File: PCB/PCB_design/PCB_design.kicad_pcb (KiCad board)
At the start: 2 copper layers, 66.5 x 66 mm, 53 parts, among them J2 Conn_01x03_Pin, J3 Conn_01x01_Pin, J4 Conn_01x01_Pin, J5 Conn_01x01_Pin, J6 Conn_01x01_Pin, J7 Conn_02x04_Counter_Clockwise, K1 Relay_SPST-NO, K2 Relay_SPST-NO, K3 Relay_SPST-NO, K4 Relay_SPST-NO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

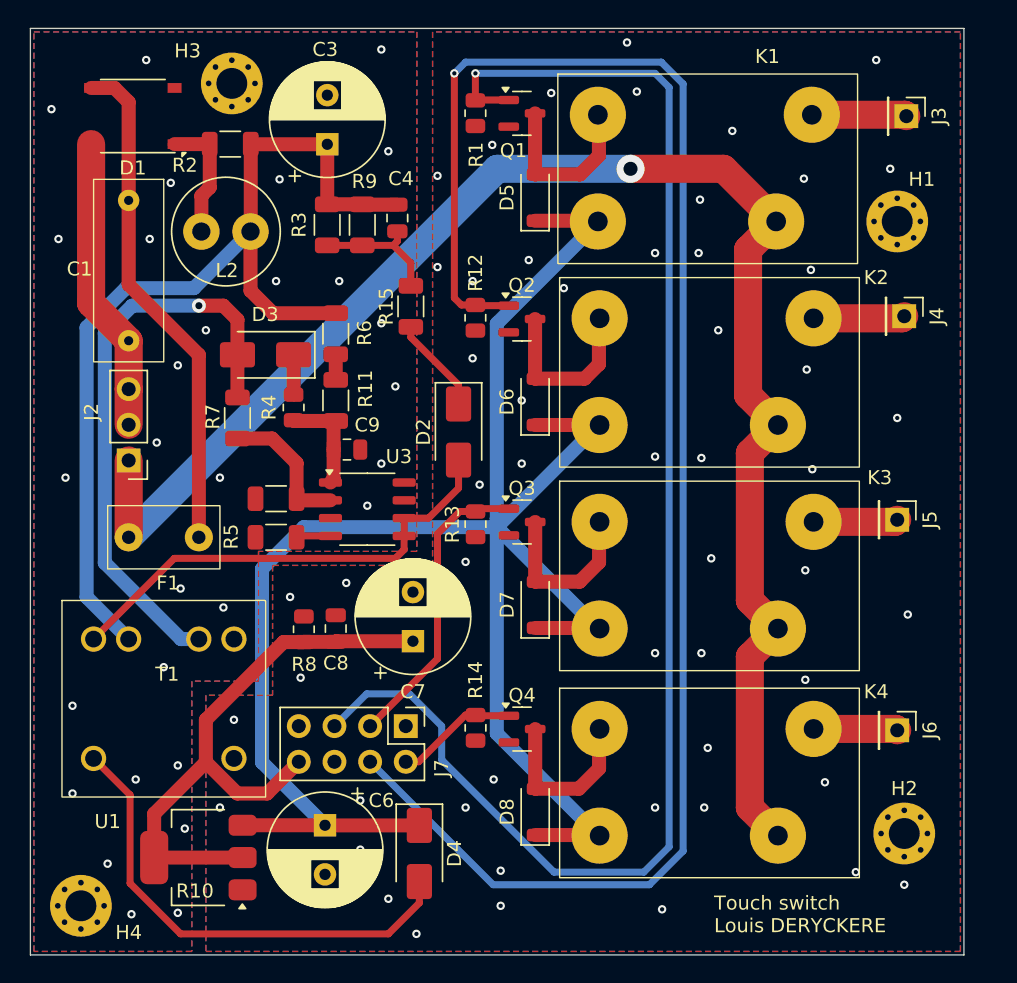
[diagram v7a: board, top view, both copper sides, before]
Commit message: Ajout pads AC & modifs pistes
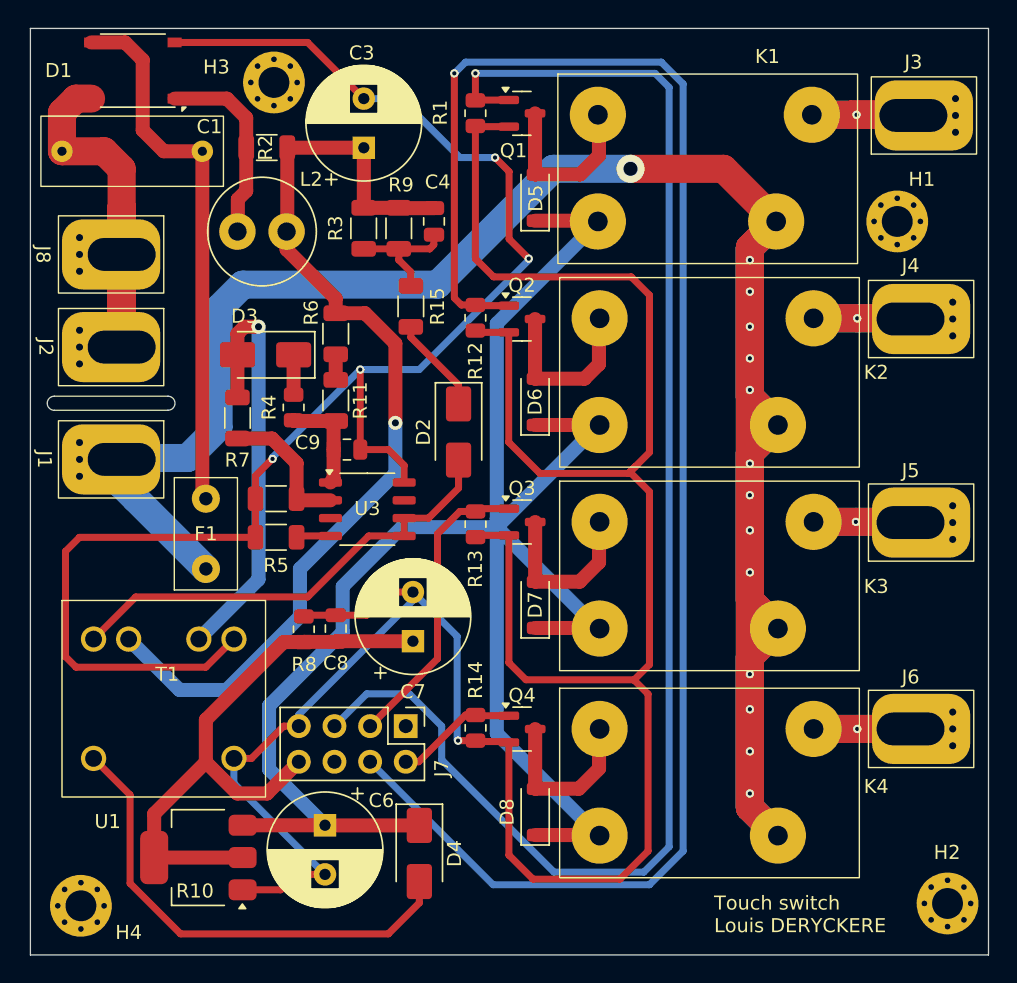
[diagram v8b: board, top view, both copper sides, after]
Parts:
- added J1: Conn_01x01_Pin, Touch_Switch_Custom:AC_pad, F.Cu at (100.0, 58.7)
- added J8: Conn_01x01_Pin, Touch_Switch_Custom:AC_pad, F.Cu at (100.0, 44.1)
- J2: value Conn_01x03_Pin -> Conn_01x01_Pin; footprint Connector_PinHeader_2.54mm:PinHeader_1x03_P2.54mm_Vertical -> Touch_Switch_Custom:AC_pad
- J3, J4, J5, J6: footprint Connector_PinHeader_2.54mm:PinHeader_1x01_P2.54mm_Vertical -> Touch_Switch_Custom:AC_pad
- moved J2 8.09 mm to (100.0, 50.7), turned to -90 degrees
- moved C1 6.31 mm to (105.8, 36.8), turned to 180 degrees
- moved H2 5.86 mm to (158.8, 90.3)
- moved D1 3.24 mm to (100.8, 31.0)
- moved F1 3.01 mm to (106.0, 64.0), turned to 90 degrees
- moved H3 3.00 mm to (110.8, 31.9)
- moved C4 2.62 mm to (122.2, 41.7)
- moved R2 2.61 mm to (110.3, 36.5)
- moved C3 2.61 mm to (117.2, 36.5)
- moved R3 2.61 mm to (117.2, 42.2)
- moved R9 2.61 mm to (119.7, 42.2)
- moved L2 2.57 mm to (108.2, 42.5)
- moved J5 0.97 mm to (156.2, 63.2), turned to 90 degrees
- moved J6 0.96 mm to (156.2, 77.9), turned to 90 degrees
- moved J3 0.50 mm to (156.4, 34.2), turned to 90 degrees
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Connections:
- J2 pad 1: L -> N
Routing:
- net GND2: track 0.00 -> 187.6 mm, vias 54 -> 1
- net L: track 113.0 -> 251.2 mm, vias 1 -> 14
- net GND: track 0.00 -> 109.9 mm, vias 30 -> 4
- net N: track 21.1 -> 41.3 mm
- net Net-(J3-Pin_1): track 7.19 -> 24.9 mm, vias 0 -> 1
- net Vaux: track 41.5 -> 30.3 mm
- net Net-(J5-Pin_1): track 6.02 -> 13.9 mm, vias 0 -> 1
- net Net-(J6-Pin_1): track 6.00 -> 13.8 mm, vias 0 -> 1
- net Net-(J4-Pin_1): track 6.52 -> 13.9 mm, vias 0 -> 1
- net Net-(D1-+): track 8.98 -> 14.3 mm
- net +5VDC: track 140.0 -> 135.4 mm
- net Net-(C1-Pad1): track 36.2 -> 38.9 mm
- net +310VDC: track 69.9 -> 71.8 mm, vias 0 -> 1
- net C: track 33.8 -> 33.2 mm
- removed copper zone on B.Cu, net GND
- removed copper zone on F.Cu, net GND
- removed copper zone on B.Cu, net GND2
- removed copper zone on F.Cu, net GND2
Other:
- board size 66.5 x 66 mm -> 68.2 x 66 mm
